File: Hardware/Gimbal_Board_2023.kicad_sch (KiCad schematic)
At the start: 70 parts, among them J1 6P6C, J2 RJ45_LED_Shielded, Q1 Q_NMOS_GDS, Q2 Q_NMOS_GDS, Q3 Q_NMOS_GDS, Q4 Q_NMOS_GDS, Q5 Q_NMOS_GDS, Q6 Q_NMOS_GDS, Q7 Q_NMOS_GDS, SW1 SW_Push, SW2 SW_Push, SW3 SW_Push, SW4 SW_Push, SW5 SW_Push, SW6 SW_Push, SW7 SW_Push, SW9 SW_DPDT_x2, U3 Teensy4.1_DEV-16771, U3.3 TSR_1-2450, U5 TSR_1-2450

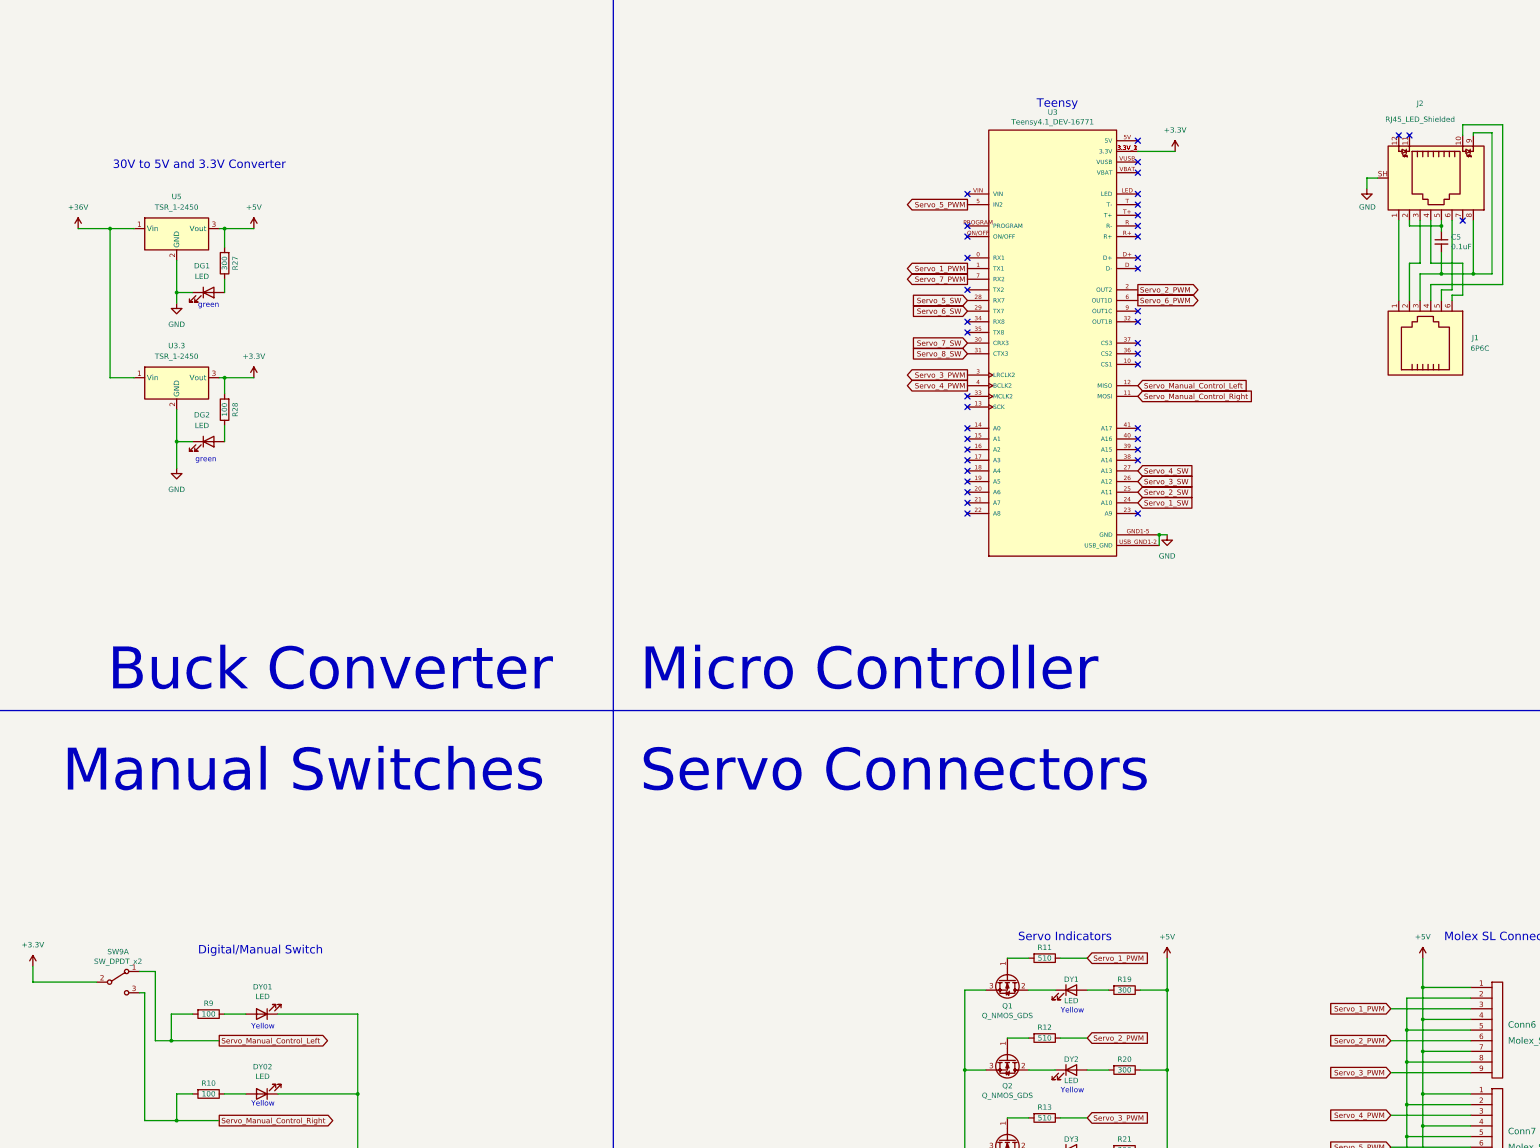
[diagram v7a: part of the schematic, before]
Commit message: changed 3v back to oki and added in capacitors, deleted servo 8 tag from teensy
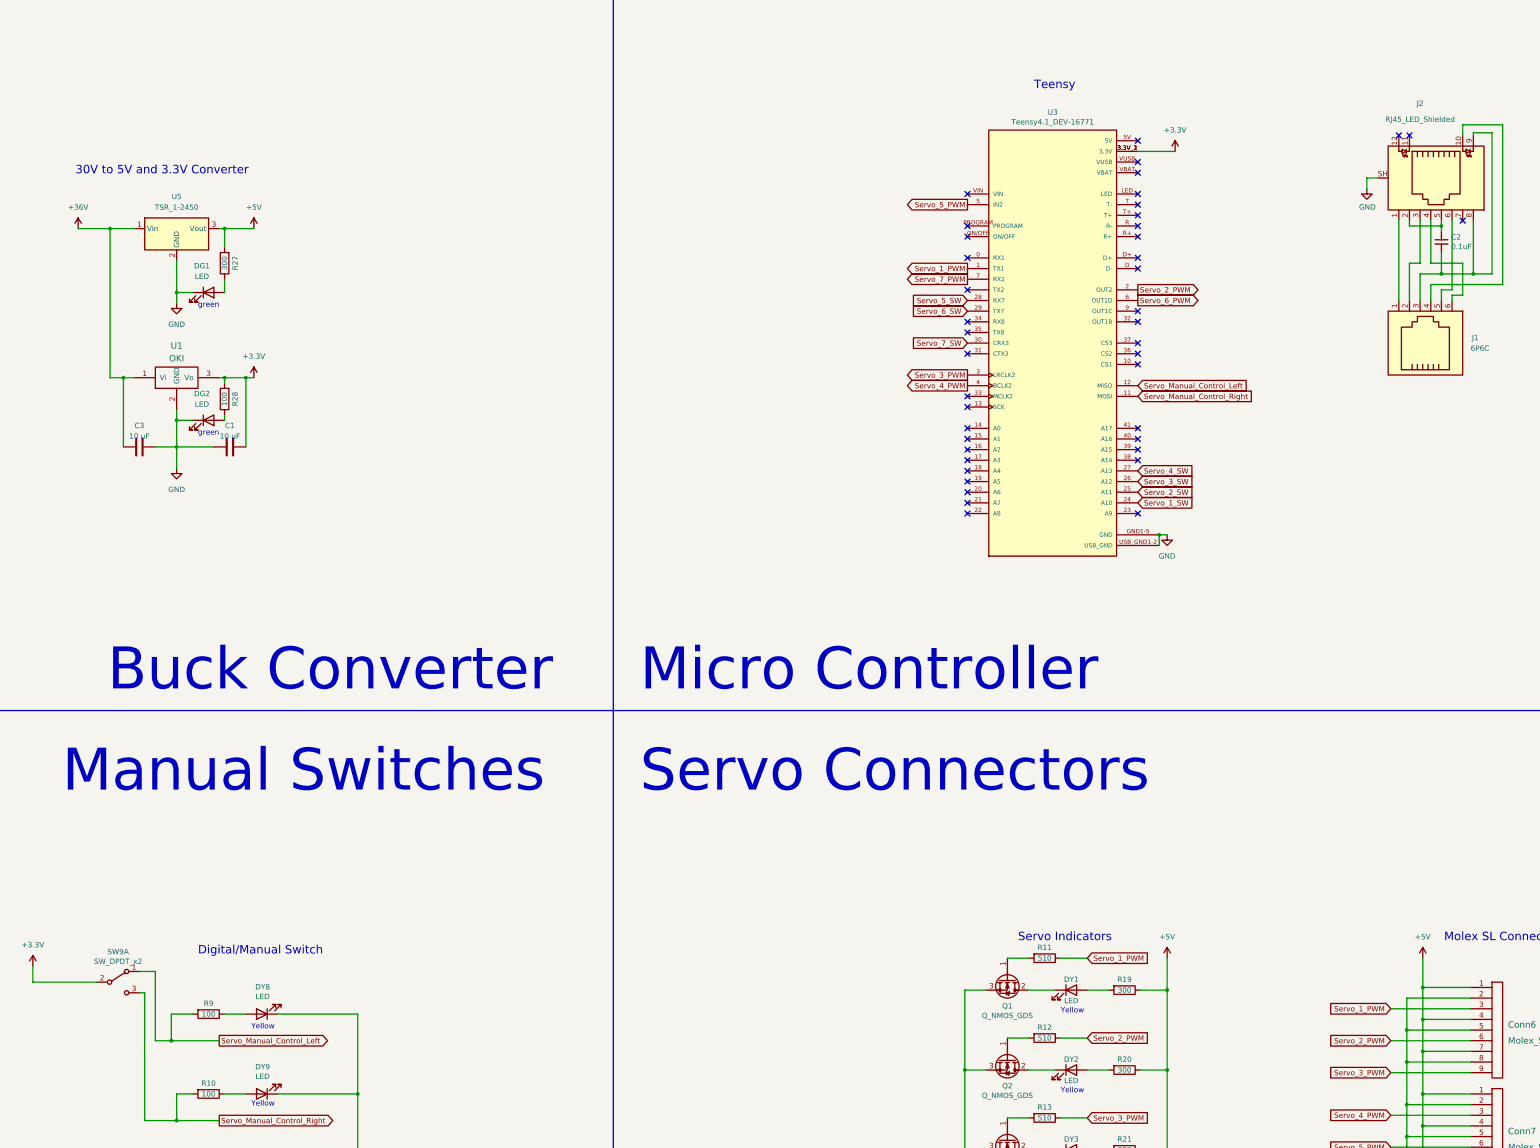
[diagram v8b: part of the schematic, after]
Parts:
- removed U3.3: TSR_1-2450, Converter_DCDC:Converter_DCDC_TRACO_TSR-1_THT, symbol Regulator_Switching:TSR_1-2450
- added C1, C3: 10 uF, symbol Device:C
- added U1: OKI, MRDT_Devices:OKI_Horizontal, symbol MRDT_Devices:OKI
- renumbered C5 to C2, DY01 to DY8, DY02 to DY9
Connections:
- net +3.3V: now also C1.2, U1.3 (Vo)
- net +36V: now also C3.1, U1.1 (Vi)
- net GND: now also C1.1, C3.2, U1.2 (GND)
- net Servo_8_SW: no longer names the net of U3.31 (CTX3)
- no-connect marks 41 -> 42
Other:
- moved on the sheet: DG2, R28
